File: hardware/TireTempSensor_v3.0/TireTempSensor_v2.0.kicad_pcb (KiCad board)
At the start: 4 copper layers, 27 x 54 mm, 57 parts, among them IC1 MAX15462AATA+, IC2 MLX90621ESF-BAB-000-SP, J1 SWD_01x06, J2 CAN_01x04, Q1 FQT3P20TF, SW1 RESET, U1 STM32L4P5RET6, U2 MIC5306-2.6YD5-TR, U3 SN65HVD232, Y1 16MGHz

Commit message: Piotruś prosił :3
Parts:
- removed F1: 200mA, Fuse:Fuse_1210_3225Metric
- removed FB4: 60R@100MHz, Inductor_SMD:L_0603_1608Metric
- removed the G*** at (102.5, 73.8)
- removed IC1: MAX15462AATA+, Package_DFN_QFN:TDFN-8-1EP_2x2mm_P0.5mm_EP0.8x1.2mm
- removed J1: SWD_01x06, Connector_PinHeader_2.54mm:PinHeader_1x06_P2.54mm_Vertical
- removed L1: 33μH, Inductor_SMD:L_Vishay_IFSC-1515AH_4x4x1.8mm
- removed R1: 100k, Resistor_SMD:R_0603_1608Metric
- added C26: 22u, Capacitor_SMD:C_0805_2012Metric_Pad1.18x1.45mm_HandSolder, F.Cu at (59.8, 179.4)
- added C27: 100n, Capacitor_SMD:C_0603_1608Metric_Pad1.08x0.95mm_HandSolder, F.Cu at (57.1, 178.9)
- added C28: 100n, Capacitor_SMD:C_0603_1608Metric_Pad1.08x0.95mm_HandSolder, F.Cu at (59.8, 181.2)
- added C29: 100n, Capacitor_SMD:C_0603_1608Metric_Pad1.08x0.95mm_HandSolder, F.Cu at (54.6, 176.0)
- added C32: 100n, Capacitor_SMD:C_0603_1608Metric_Pad1.08x0.95mm_HandSolder, F.Cu at (56.5, 124.8)
- added C33: 47u, Capacitor_SMD:C_0603_1608Metric_Pad1.08x0.95mm_HandSolder, F.Cu at (56.5, 127.3)
- added C34: 47u, Capacitor_SMD:C_0603_1608Metric_Pad1.08x0.95mm_HandSolder, F.Cu at (56.5, 129.8)
- added C35: 220n, Capacitor_SMD:C_0603_1608Metric_Pad1.08x0.95mm_HandSolder, F.Cu at (56.5, 132.3)
- added C36: 100n, Capacitor_SMD:C_0603_1608Metric_Pad1.08x0.95mm_HandSolder, F.Cu at (56.5, 134.8)
- added C37: 10n, Capacitor_SMD:C_0603_1608Metric_Pad1.08x0.95mm_HandSolder, F.Cu at (60.8, 124.8)
- added C38: 100n, Capacitor_SMD:C_0603_1608Metric_Pad1.08x0.95mm_HandSolder, F.Cu at (60.8, 127.3)
- added C39: 10n, Capacitor_SMD:C_0603_1608Metric_Pad1.08x0.95mm_HandSolder, F.Cu at (60.8, 129.8)
- added C40: 100n, Capacitor_SMD:C_0603_1608Metric_Pad1.08x0.95mm_HandSolder, F.Cu at (62.2, 184.5)
- added C41: 22u, Capacitor_SMD:C_0805_2012Metric_Pad1.18x1.45mm_HandSolder, F.Cu at (64.9, 183.8)
- added C42: 22u, Capacitor_SMD:C_0805_2012Metric_Pad1.18x1.45mm_HandSolder, F.Cu at (64.9, 185.8)
- added C43: 22u, Capacitor_SMD:C_0805_2012Metric_Pad1.18x1.45mm_HandSolder, F.Cu at (64.9, 187.8)
- added C44: 10u, Capacitor_SMD:C_0603_1608Metric_Pad1.08x0.95mm_HandSolder, F.Cu at (58.0, 176.1)
- added C45: 22u, Capacitor_SMD:C_0805_2012Metric_Pad1.18x1.45mm_HandSolder, F.Cu at (51.0, 175.8)
- added D10: D_TVS_Dual_AAC, Package_TO_SOT_SMD:SOT-23_Handsoldering, F.Cu at (72.1, 155.9)
- added D11: D_Zener, Diode_SMD:D_SOD-123, F.Cu at (82.3, 156.2)
- added D12: D_Zener, Diode_SMD:D_SOD-123, F.Cu at (82.3, 159.5)
- added D13: +3V3, LED_SMD:LED_0603_1608Metric_Pad1.05x0.95mm_HandSolder, F.Cu at (52.5, 184.8)
- added D7: D_TVS_Dual_AAC, Package_TO_SOT_SMD:SOT-23_Handsoldering, F.Cu at (72.1, 142.2)
- added D8: D_TVS_Dual_AAC, Package_TO_SOT_SMD:SOT-23_Handsoldering, F.Cu at (72.1, 146.8)
- added D9: D_TVS_Dual_AAC, Package_TO_SOT_SMD:SOT-23_Handsoldering, F.Cu at (72.1, 151.3)
- added F2: F0603G0R05FNTR, Fuse:Fuse_0603_1608Metric_Pad1.05x0.95mm_HandSolder, F.Cu at (56.0, 151.3)
- added F3: F0603G0R05FNTR, Fuse:Fuse_0603_1608Metric_Pad1.05x0.95mm_HandSolder, F.Cu at (48.3, 175.1)
- added F4: F0603G0R05FNTR, Fuse:Fuse_0603_1608Metric_Pad1.05x0.95mm_HandSolder, F.Cu at (54.6, 187.9)
- added F5: F0603G0R05FNTR, Fuse:Fuse_0603_1608Metric_Pad1.05x0.95mm_HandSolder, F.Cu at (59.7, 177.6)
- added FB5: 2K@100MHz, Inductor_SMD:L_0603_1608Metric_Pad1.05x0.95mm_HandSolder, F.Cu at (60.8, 132.3)
- added FB6: 2K@100MHz, Inductor_SMD:L_0603_1608Metric_Pad1.05x0.95mm_HandSolder, F.Cu at (60.8, 134.8)
- added FB7: 2K@100MHz, Inductor_SMD:L_0603_1608Metric_Pad1.05x0.95mm_HandSolder, F.Cu at (65.2, 124.8)
- added FB8: 2K@100MHz, Inductor_SMD:L_0603_1608Metric_Pad1.05x0.95mm_HandSolder, F.Cu at (65.2, 127.3)
- added IC4: TPS54202HDDCR, Package_TO_SOT_SMD:SOT-23-6_Handsoldering, F.Cu at (59.7, 184.3)
- added L4: 68u/1A4, Inductor_SMD:L_TDK_VLS6045EX_VLS6045AF, F.Cu at (65.0, 179.5)
- added R14: 1k, Resistor_SMD:R_0603_1608Metric_Pad0.98x0.95mm_HandSolder, F.Cu at (49.1, 184.8)
- added R15: 10k, Resistor_SMD:R_0603_1608Metric, F.Cu at (77.3, 141.2)
- added R16: 10k, Resistor_SMD:R_0603_1608Metric, F.Cu at (77.3, 143.7)
- added R17: 10k, Resistor_SMD:R_0603_1608Metric, F.Cu at (77.3, 146.2)
- added R18: 1k, Resistor_SMD:R_0603_1608Metric, F.Cu at (77.3, 148.8)
- added R19: 1k, Resistor_SMD:R_0603_1608Metric, F.Cu at (77.3, 151.3)
- added R20: 1k, Resistor_SMD:R_0603_1608Metric, F.Cu at (77.3, 153.8)
- added R21: 100K, Resistor_SMD:R_0603_1608Metric_Pad0.98x0.95mm_HandSolder, F.Cu at (65.2, 129.8)
- added R22: 510k, Resistor_SMD:R_0603_1608Metric_Pad0.98x0.95mm_HandSolder, F.Cu at (57.1, 184.5)
- added R23: 13.2k, Resistor_SMD:R_0603_1608Metric_Pad0.98x0.95mm_HandSolder, F.Cu at (58.0, 187.5)
- added R24: 100k, Resistor_SMD:R_0603_1608Metric_Pad0.98x0.95mm_HandSolder, F.Cu at (61.3, 187.5)
- added SW2: 3 pos dip switch, footprint:DS04254103BKSMT, F.Cu at (85.6, 146.9)
- added T10: TP_+5V, TestPoint:TestPoint_Pad_1.0x1.0mm, B.Cu at (59.6, 177.8)
- added T12: TP_+5V, TestPoint:TestPoint_Pad_1.0x1.0mm, B.Cu at (63.9, 187.8)
- added T13: TP_+5V, TestPoint:TestPoint_Pad_1.0x1.0mm, F.Cu at (58.4, 154.1)
- added T14: TP_+3.3V, TestPoint:TestPoint_Pad_1.0x1.0mm, B.Cu at (50.0, 173.9)
- added T15: TP_+2.6V, TestPoint:TestPoint_Pad_1.0x1.0mm, B.Cu at (55.5, 189.6)
- added U7: ADM3057ExRW, Package_SO:SOIC-20W_7.5x12.8mm_P1.27mm, F.Cu at (30.9, 139.7)
- C12, C13: value 1u -> 100n
- C16: value 10u -> 100n; footprint Capacitor_SMD:C_1206_3216Metric -> Capacitor_SMD:C_0603_1608Metric
- D1: value PESD2CAN,215 -> 30V; footprint Package_TO_SOT_SMD:SOT-23 -> Diode_SMD:D_SOD-123
- IC2: moved to F.Cu
- U1: value STM32L4P5RET6 -> STM32G0C1KCTxN; footprint Package_QFP:LQFP-64_10x10mm_P0.5mm -> Package_QFP:LQFP-32_7x7mm_P0.8mm
- U3: value SN65HVD232 -> LM1117-3.3; footprint Package_SO:SOIC-8_3.9x4.9mm_P1.27mm -> Package_TO_SOT_SMD:SOT-223-3_TabPin2
- moved C14 136.4 mm to (48.9, 189.5), turned to 0 degrees
- moved U2 132.7 mm to (50.8, 187.3), turned to 0 degrees
- moved FB2 132.0 mm to (48.0, 187.3), turned to -90 degrees
- moved C15 128.3 mm to (54.4, 186.4), turned to 0 degrees
- moved U3 95.0 mm to (51.9, 180.4), turned to 180 degrees
- moved U1 80.1 mm to (40.8, 118.0), turned to -135 degrees
- moved C16 55.5 mm to (80.3, 69.8), turned to 0 degrees
- moved J2 53.9 mm to (72.1, 85.4), turned to 0 degrees
- moved H1 49.4 mm to (96.1, 71.5)
- moved C13 49.3 mm to (76.3, 82.3)
- moved C4 48.5 mm to (72.3, 77.3), turned to 0 degrees
- moved IC2 48.3 mm to (79.0, 101.4), turned to 0 degrees
- moved R6 47.4 mm to (84.7, 104.0), turned to 0 degrees
- moved C11 47.4 mm to (76.3, 77.3), turned to 0 degrees
- moved C12 47.3 mm to (76.3, 79.8)
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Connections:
- C12 pad 1: /Power Supply 3.3v 2.6v/+24V safe -> /Switch1
- C13 pad 1: Net-(C13-Pad1) -> /Switch2
- C15 pad 1: +2V6 -> Net-(U2-VOUT)
- C16 pad 1: +3V3 -> /Switch3
- D1 pad 1: /CAN - -> +24V
- D1 pad 2: /CAN + -> GND
- JP1 pad 1: Net-(F1-Pad2) -> Net-(JP1-A)
- U1 pad 1: /+3V3_uC -> unconnected-(U1-PB9-Pad1)
- U1 pad 12: GND -> /LED OK
- U1 pad 13: /+3V3_uC -> /LED ERR
- U1 pad 14: unconnected-(U1-Pad14) -> /LED WAR1
- U1 pad 16: /LED WAR2 -> unconnected-(U1-PB1-Pad16)
- U1 pad 18: GND -> /LED WAR2
- U1 pad 19: /+3V3_uC -> /Switch1
- U1 pad 2: unconnected-(U1-Pad2) -> /OSC IN
- U1 pad 20: unconnected-(U1-Pad20) -> /+3V3_uC
- U1 pad 21: unconnected-(U1-Pad21) -> /Switch2
- U1 pad 22: /LED ERR -> /Switch3
- U1 pad 24: /LED WAR1 -> /SWDIO
- U1 pad 25: unconnected-(U1-Pad25) -> /SWCLK
- U1 pad 26: /LED OK -> /STBY_CAN
- U1 pad 29: /SCL -> unconnected-(U1-PD3-Pad29)
- U1 pad 3: unconnected-(U1-Pad3) -> /OSC OUT
- U1 pad 30: /SDA -> unconnected-(U1-PB6-Pad30)
- U1 pad 31: GND -> unconnected-(U1-PB7-Pad31)
- U1 pad 32: /+3V3_uC -> unconnected-(U1-PB8-Pad32)
- U1 pad 4: unconnected-(U1-Pad4) -> /+3V3_uC
- U1 pad 5: /OSC IN -> GND
- U1 pad 6: /OSC OUT -> /NRST
- U1 pad 7: /NRST -> unconnected-(U1-PA0-Pad7)
- U1 pad 8: unconnected-(U1-Pad8) -> /SCL
- U1 pad 9: unconnected-(U1-Pad9) -> /SDA
- U2 pad 5: +2V6 -> Net-(U2-VOUT)
- U3 pad 1: /CAN TX -> GND
- U3 pad 2: GND -> /Power Supply 3.3v 2.6v/VO_+3.3V
- U3 pad 3: Net-(FB4-Pad2) -> +5V
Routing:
- net GND: track 54.2 -> 0.00 mm, vias 42 -> 0
- net /SWO: track 30.5 -> 0.00 mm
- net /CAN RX: track 30.5 -> 0.00 mm, vias 2 -> 0
- net /NRST: track 29.3 -> 0.00 mm
- net /CAN TX: track 27.7 -> 0.00 mm, vias 2 -> 0
- net /SCL: track 25.8 -> 0.00 mm, vias 2 -> 0
- net /SDA: track 24.7 -> 0.00 mm, vias 2 -> 0
- net /+3V3_uC: track 20.4 -> 0.00 mm, vias 8 -> 0
- net /CAN +: track 16.7 -> 0.00 mm
- net /CAN -: track 15.4 -> 0.00 mm
- net +2V6: track 12.9 -> 0.00 mm
- net /SWDIO: track 12.4 -> 0.00 mm
- net /SWCLK: track 12.0 -> 0.00 mm, vias 2 -> 0
- net /OSC IN: track 10.5 -> 0.00 mm
- net /LED OK: track 10.3 -> 0.00 mm
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- removed copper zone on F.Cu, net +3V3
- removed copper zone on In2.Cu, net +3V3
- removed copper zone on In2.Cu, net /+3V3_uC
- removed copper zone on F.Cu, net /Power Supply 3.3v 2.6v/+24V safe
- removed copper zone on B.Cu, net GND
- removed copper zone on F.Cu, net GND
- removed copper zone on In1.Cu, net GND
- removed copper zone on F.Cu, net Net-(C13-Pad1)
- removed copper zone on F.Cu, net Net-(F1-Pad2)
- removed copper zone on F.Cu, net Net-(IC1-Pad8)
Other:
- board size 27 x 54 mm -> 25.8 x 20.6 mm

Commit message: Poprawki, kontynuacja layoutu
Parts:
- removed C16: 100n, Capacitor_SMD:C_0603_1608Metric
- removed R17: 10k, Resistor_SMD:R_0603_1608Metric
- removed R20: 1k, Resistor_SMD:R_0603_1608Metric
- removed SW2: 3 pos dip switch, footprint:DS04254103BKSMT
- added D14: D_TVS_Dual_AAC, Package_TO_SOT_SMD:SOT-23_Handsoldering, F.Cu at (128.3, 100.1)
- added D15: D_TVS_Dual_AAC, Package_TO_SOT_SMD:SOT-23_Handsoldering, F.Cu at (132.9, 101.0)
- added J3: FTSH-107-01-L-D-K, footprint:FTSH-107-XX-YYY-DV-K, F.Cu at (131.2, 93.8)
- added SW3: SW_DIP_x02, footprint:2192LPST, B.Cu at (155.3, 99.6)
- C32, C38: value 100n -> 47u
- C35: value 220n -> 47u
- IC2, R15, R16, R18, R19: moved to B.Cu
- J2: value CAN_01x04 -> Main connector; footprint Connector_Wire:SolderWire-0.1sqmm_1x04_P3.6mm_D0.4mm_OD1mm_Relief -> footprint:M80-51004YY
- Q1: footprint Mosfet:SOT-223-4-NFET -> Package_TO_SOT_SMD:SOT-223-3_TabPin2
- moved F3 140.4 mm to (161.7, 92.3), turned to 180 degrees
- moved T10 139.3 mm to (172.3, 96.0)
- moved T12 139.3 mm to (176.7, 106.0)
- moved T15 139.3 mm to (168.2, 107.8)
- moved C26 139.3 mm to (172.5, 97.7)
- moved C27 139.3 mm to (169.8, 97.1)
- moved C45 139.3 mm to (163.7, 94.0)
- moved D13 139.3 mm to (165.2, 103.0)
- moved F5 139.3 mm to (172.4, 95.8)
- moved FB2 139.3 mm to (160.7, 105.5)
- moved IC4 139.3 mm to (172.4, 102.6)
- moved R14 139.3 mm to (161.8, 103.0)
- moved U2 139.3 mm to (163.5, 105.5)
- moved C14 139.3 mm to (161.6, 107.8)
- moved C15 139.3 mm to (167.2, 104.7)
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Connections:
- D10 pad 1: /OSC IN -> /OSC OUT
- D10 pad 2: /OSC OUT -> /OSC IN
- D7 pad 1: /SCL -> /SDA
- D7 pad 2: /SDA -> /SCL
- D8 pad 1: /SWDIO -> /SWCLK
- D8 pad 2: /SWCLK -> /SWDIO
- J2 pad 3: /CAN + -> /CAN -
- J2 pad 4: /CAN - -> /CAN +
- U1 pad 1: unconnected-(U1-PB9-Pad1) -> /CAN TX
- U1 pad 10: unconnected-(U1-PA3-Pad10) -> /LED OK
- U1 pad 11: unconnected-(U1-PA4-Pad11) -> /LED ERR
- U1 pad 12: /LED OK -> /LED WAR1
- U1 pad 13: /LED ERR -> /LED WAR2
- U1 pad 14: /LED WAR1 -> unconnected-(U1-PA7-Pad14)
- U1 pad 18: /LED WAR2 -> unconnected-(U1-PA8-Pad18)
- U1 pad 22: /Switch3 -> /CAN RX
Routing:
- net /Power Supply 3.3v 2.6v/+24V safe: track 0.00 -> 35.7 mm, vias 0 -> 2
- net /+3V3_uC: track 0.00 -> 21.0 mm
- net /SDA: track 0.00 -> 16.8 mm
- net /SCL: track 0.00 -> 16.0 mm
- net /NRST: track 0.00 -> 15.6 mm
- net /OSC OUT: track 0.00 -> 13.2 mm
- net /Power Supply 3.3v 2.6v/VO_+3.3V: track 0.00 -> 13.0 mm
- net /Power Supply 3.3v 2.6v/+5V_OUT: track 0.00 -> 12.6 mm, vias 0 -> 1
- net /OSC IN: track 0.00 -> 12.1 mm
- net +3V3: track 0.00 -> 9.59 mm
- net /Power Supply 3.3v 2.6v/SW_+5V: track 0.00 -> 8.44 mm
- net Net-(R3-Pad1): track 0.00 -> 7.31 mm
- net Net-(U2-EN): track 0.00 -> 6.91 mm
- net /SWDIO: track 0.00 -> 6.23 mm
- net /Switch2: track 0.00 -> 6.05 mm
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- added copper zone on F.Cu, net /Power Supply 3.3v 2.6v/+5V_OUT
- added copper zone on F.Cu, net /Power Supply 3.3v 2.6v/VO_+3.3V
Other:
- board outline removed

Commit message: Propozycja layoutu na spotkanie
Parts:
- removed D3, D4: YELLOW, Diode_SMD:D_0603_1608Metric
- removed D6: RED, Diode_SMD:D_0603_1608Metric
- removed JP1: SolderJumper_2_Open, Jumper:SolderJumper-2_P1.3mm_Open_TrianglePad1.0x1.5mm
- removed Q1: FQT3P20TF, Package_TO_SOT_SMD:SOT-223-3_TabPin2
- removed R10, R7, R8: 1k5, Resistor_SMD:R_0603_1608Metric
- added D16: D_Schottky, Diode_SMD:D_SOD-882D, F.Cu at (177.2, 108.2)
- T13: moved to B.Cu
- moved C33 76.9 mm to (129.7, 103.8), turned to 90 degrees
- moved C32 73.8 mm to (127.3, 104.2)
- moved C38 70.0 mm to (127.7, 106.6)
- moved T13 68.3 mm to (127.7, 106.6)
- moved FB7 65.9 mm to (127.3, 102.7)
- moved C36 64.7 mm to (111.3, 100.6)
- moved C39 64.5 mm to (121.0, 106.6), turned to 180 degrees
- moved C34 62.9 mm to (111.3, 99.1), turned to 180 degrees
- moved FB8 62.7 mm to (124.4, 106.6)
- moved C35 61.9 mm to (111.3, 103.6)
- moved C37 60.0 mm to (111.4, 92.5)
- moved FB5 58.9 mm to (111.3, 102.1), turned to 180 degrees
- moved FB6 58.6 mm to (111.4, 105.1)
- moved R21 58.5 mm to (111.4, 94.0)
- moved R6 54.6 mm to (139.2, 100.7)
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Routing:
- net /Power Supply 3.3v 2.6v/+24V safe: track 35.7 -> 19.2 mm
- net Net-(D16-A): track 4.63 -> 1.87 mm
- net /NRST: track 15.6 -> 17.0 mm
- net /SDA: track 16.8 -> 16.2 mm
- added copper zone on B.Cu, net GND
- added copper zone on F.Cu, net GND
- added copper zone on In1.Cu, net GND
- added copper zone on In2.Cu, net GND
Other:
- board outline added: 82.5 x 20.6 mm

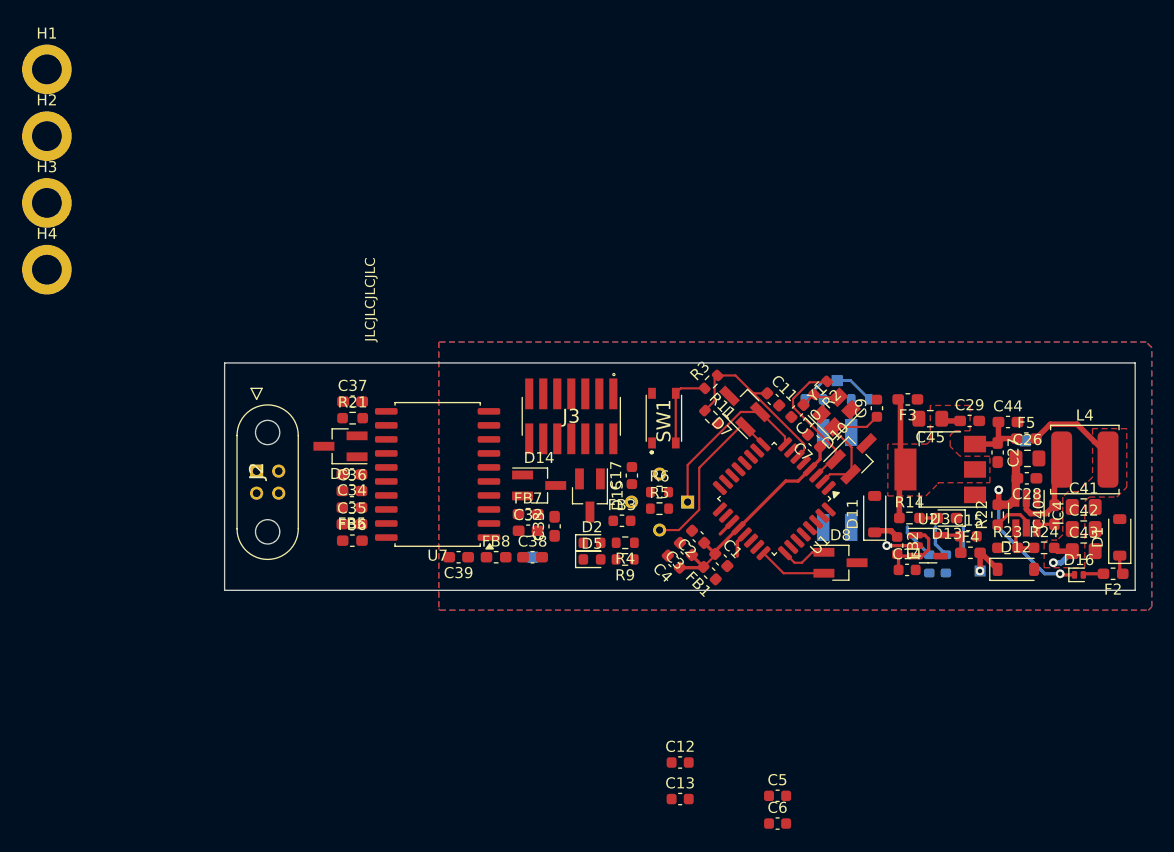
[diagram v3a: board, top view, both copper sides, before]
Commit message: Nowy layout, nowe tvsy
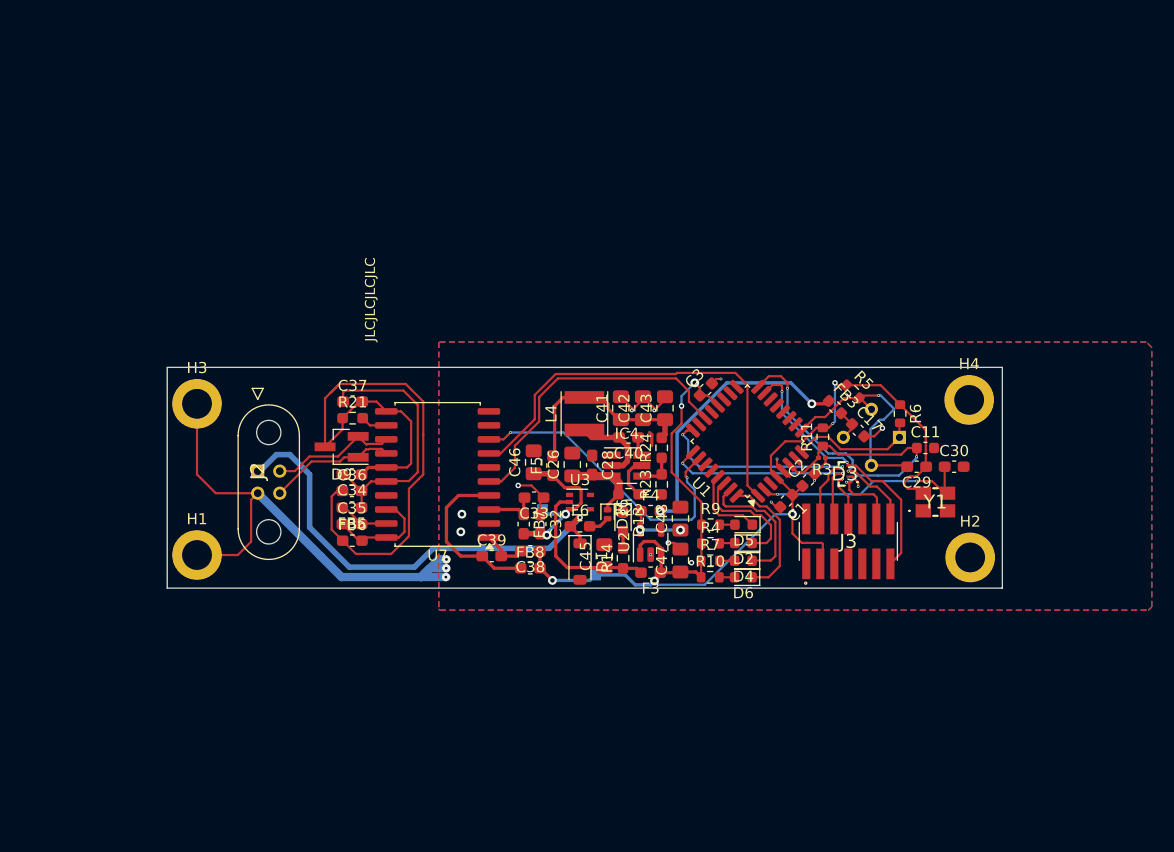
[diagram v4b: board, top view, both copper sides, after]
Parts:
- removed C10, C9: 8p, Capacitor_SMD:C_0603_1608Metric
- removed C12, C13, C14, C15, C4, C5, C6, C7: 100n, Capacitor_SMD:C_0603_1608Metric
- removed C27: 100n, Capacitor_SMD:C_0603_1608Metric_Pad1.08x0.95mm_HandSolder
- removed C44: 10u, Capacitor_SMD:C_0603_1608Metric_Pad1.08x0.95mm_HandSolder
- removed D10, D14, D15, D7, D8: D_TVS_Dual_AAC, Package_TO_SOT_SMD:SOT-23_Handsoldering
- removed D11, D12: D_Zener, Diode_SMD:D_SOD-123
- removed F2: F0603G0R05FNTR, Fuse:Fuse_0603_1608Metric_Pad1.05x0.95mm_HandSolder
- removed FB1, FB2: 60R@100MHz, Inductor_SMD:L_0603_1608Metric
- removed R15, R16: 10k, Resistor_SMD:R_0603_1608Metric
- removed R18, R19: 1k, Resistor_SMD:R_0603_1608Metric
- removed R2: 47, Resistor_SMD:R_0603_1608Metric
- removed SW1: RESET, Button:PTS815SJK250SMTRLFS
- removed SW3: SW_DIP_x02, footprint:2192LPST
- removed T12, T13: TP_+5V, TestPoint:TestPoint_Pad_1.0x1.0mm
- added C30: 6p, Capacitor_SMD:C_0603_1608Metric_Pad1.08x0.95mm_HandSolder, F.Cu at (165.9, 98.4)
- added C46: 22u, Capacitor_SMD:C_0805_2012Metric_Pad1.18x1.45mm_HandSolder, F.Cu at (127.8, 98.0)
- added C47: 22u, Capacitor_SMD:C_0805_2012Metric_Pad1.18x1.45mm_HandSolder, F.Cu at (141.1, 106.9)
- added C48: 22u, Capacitor_SMD:C_0805_2012Metric_Pad1.18x1.45mm_HandSolder, F.Cu at (141.1, 103.1)
- added D3: PUSB3AB6Z, footprint:PUSB3AB6Z, F.Cu at (156.0, 99.0)
- added D4: RED, Diode_SMD:D_0603_1608Metric, F.Cu at (146.8, 106.9)
- added D6: GREEN, Diode_SMD:D_0603_1608Metric, F.Cu at (146.8, 108.4)
- added F6: SF-0603FP050M-2, Fuse:Fuse_0603_1608Metric_Pad1.05x0.95mm_HandSolder, F.Cu at (132.0, 103.8)
- added R10: 1k5, Resistor_SMD:R_0603_1608Metric, F.Cu at (143.8, 108.4)
- added R7: 1k5, Resistor_SMD:R_0603_1608Metric, F.Cu at (143.8, 106.9)
- C29: value 100n -> 100nF
- F5: value F0603G0R05FNTR -> SF-0603FP050M-2
- L4: footprint Inductor_SMD:L_TDK_VLS6045EX_VLS6045AF -> Inductor_SMD:L_Vishay_IFSC-1515AH_4x4x1.8mm
- R3: value 1k -> NC; footprint Resistor_SMD:R_0603_1608Metric -> Resistor_SMD:R_0201_0603Metric
- U3: value LM1117-3.3 -> NCP715SQ33T2G; footprint Package_TO_SOT_SMD:SOT-223-3_TabPin2 -> Package_TO_SOT_SMD:SOT-353_SC-70-5
- Y1: value 16MGHz -> ATX-11-F-32.000MHZ-F05-T; footprint Crystal:Crystal_SMD_SeikoEpson_TSX3225-4Pin_3.2x2.5mm -> footprint:ATX11F32000MHZF05T
- moved H2 91.9 mm to (167.3, 106.6)
- moved H4 84.4 mm to (167.3, 92.3)
- moved D1 48.9 mm to (132.0, 107.0), turned to -90 degrees
- moved H1 46.1 mm to (97.3, 106.4)
- moved L4 45.5 mm to (132.4, 93.6), turned to 90 degrees
- moved T10 44.2 mm to (128.6, 102.3)
- moved D16 43.1 mm to (134.5, 102.7), turned to -90 degrees
- moved F5 43.0 mm to (129.5, 98.3), turned to 90 degrees
- moved C41 42.9 mm to (135.7, 93.1), turned to 90 degrees
- moved C42 41.4 mm to (137.7, 93.1), turned to 90 degrees
- moved C26 41.2 mm to (131.3, 98.2), turned to 90 degrees
- moved C43 40.1 mm to (139.7, 93.1), turned to 90 degrees
- moved C28 39.4 mm to (133.1, 98.2), turned to -90 degrees
- moved C40 39.2 mm to (136.4, 95.8), turned to 180 degrees
- moved IC4 36.4 mm to (136.2, 98.3), turned to 0 degrees
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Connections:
- C1 pad 1: /+3V3_uC -> +3V3
- C2 pad 1: /+3V3_uC -> +3V3
- C29 pad 1: /Power Supply 3.3v 2.6v/VO_+3.3V -> +3V3
- C3 pad 1: /+3V3_uC -> +3V3
- C38 pad 1: +3.3V -> +3V3
- D2 pad 1: GND -> /LED ERR
- D5 pad 1: GND -> /LED OK
- FB8 pad 2: +3.3V -> +3V3
- J3 pad 13: unconnected-(J3-Pin_13-Pad13) -> /URAT_RX
- J3 pad 14: unconnected-(J3-Pin_14-Pad14) -> /URAT_TX
- J3 pad 3: +3.3V -> +3V3
- R3 pad 1: Net-(R3-Pad1) -> GND
- R4 pad 1: /LED ERR -> +3V3
- R9 pad 1: /LED OK -> +3V3
- U1 pad 10: /LED OK -> unconnected-(U1-PA3-Pad10)
- U1 pad 11: /LED ERR -> unconnected-(U1-PA4-Pad11)
- U1 pad 15: unconnected-(U1-PB0-Pad15) -> /URAT_RX
- U1 pad 16: unconnected-(U1-PB1-Pad16) -> /URAT_TX
- U1 pad 20: /+3V3_uC -> +3V3
- U1 pad 29: unconnected-(U1-PD3-Pad29) -> /LED OK
- U1 pad 30: unconnected-(U1-PB6-Pad30) -> /LED ERR
- U1 pad 31: unconnected-(U1-PB7-Pad31) -> /LED_ADRESS_INDICATOR_1
- U1 pad 32: unconnected-(U1-PB8-Pad32) -> /LED_ADRESS_INDICATOR_2
- U1 pad 4: /+3V3_uC -> +3V3
- U2 pad 1: Net-(U2-EN) -> +3V3
- U2 pad 3: Net-(U2-EN) -> +3V3
- Y1 pad 1: /OSC IN -> GND
- Y1 pad 3: Net-(C10-Pad1) -> /OSC IN
- Y1 pad 4: GND -> +3V3
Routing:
- net +3V3: track 9.59 -> 105.3 mm, vias 0 -> 7
- net GND: track 2.61 -> 79.4 mm, vias 1 -> 18
- net /GND_ISO: track 0.00 -> 60.5 mm
- net +24V: track 1.76 -> 41.8 mm, vias 0 -> 1
- net /CAN TX: track 0.00 -> 38.6 mm
- net /STBY_CAN: track 0.00 -> 28.4 mm, vias 0 -> 2
- net /CAN RX: track 0.00 -> 28.0 mm
- net /URAT_RX: track 0.00 -> 24.7 mm, vias 0 -> 2
- net Net-(U7-VISOIN): track 0.00 -> 24.0 mm
- net +2V6: track 3.86 -> 25.5 mm, vias 1 -> 2
- net /URAT_TX: track 0.00 -> 21.5 mm, vias 0 -> 2
- net /+3V3_uC: track 21.0 -> 0.00 mm
- net /SWDIO: track 6.23 -> 23.5 mm, vias 0 -> 2
- net /SWCLK: track 4.28 -> 21.1 mm, vias 0 -> 2
- net Net-(U7-VIO): track 0.00 -> 15.1 mm
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- removed copper zone on F.Cu, net /Power Supply 3.3v 2.6v/+5V_OUT
- removed copper zone on F.Cu, net /Power Supply 3.3v 2.6v/VO_+3.3V
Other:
- board size 82.5 x 20.6 mm -> 75.7 x 20 mm
- board text added: "Wiktor Krakowski :3"

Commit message: Gotowe do sprawdzenia
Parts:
- R3: footprint Resistor_SMD:R_0201_0603Metric -> Resistor_SMD:R_0402_1005Metric
- moved C1 1.33 mm to (150.9, 102.8), turned to -90 degrees
- moved R3 1.27 mm to (153.3, 98.7), turned to 135 degrees
- moved H1 1.26 mm to (98.5, 106.0)
- moved H3 1.20 mm to (98.5, 92.7)
- moved C2 1.05 mm to (152.3, 100.6), turned to 0 degrees
- moved Y1 0.55 mm to (164.8, 101.6)
- moved C48 0.14 mm to (141.2, 103.1)
- moved F5 0.06 mm to (129.6, 98.3)
- moved D13 0.06 mm to (136.0, 103.4)
- moved R14 0.05 mm to (135.9, 106.8)
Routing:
- net GND: track 79.4 -> 82.8 mm, vias 18 -> 25
- net /SDA: track 18.0 -> 16.5 mm
- net +24V: track 41.8 -> 40.7 mm
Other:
- board size 75.7 x 20 mm -> 75 x 20.5 mm
- board text added: "bridge to rst"

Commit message: Do sprawdzenia :3
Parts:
- moved G*** 4.97 mm to (118.5, 95.5)
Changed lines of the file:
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@@
 		(tags "SOT-23")
 		(property "Reference" "D9"
-			(at 2.25 -0.11 180)
+			(at 2.4 1.1 180)
 			(layer "F.SilkS")
 			(effects
@@
 		(tags "test point SMD pad rectangle square")
 		(property "Reference" "T10"
-			(at 2.4 0.7 180)
+			(at 2.4 0.2 180)
 			(layer "B.SilkS")
 			(effects
@@
 		(tags "test point SMD pad rectangle square")
 		(property "Reference" "T14"
-			(at 0 1.448 180)
+			(at -2.4 -0.2 180)
 			(layer "B.SilkS")
 			(effects
@@
 	(footprint "mylogo:logo"
 		(layer "B.Cu")
-		(at 120.6 100 180)
+		(at 118.5 95.5 180)
 		(property "Reference" "G***"
 			(at -0.5 4.75 0)
@@
 		(tags "test point SMD pad rectangle square")
 		(property "Reference" "T15"
-			(at 0 1.448 180)
+			(at -2.2 -0.1 180)
 			(layer "B.SilkS")
 			(effects
@@
 	)
 	(gr_line
-		(start 120.5 104.5)
-		(end 121.5 105.5)
+		(start 117.5 100)
+		(end 118.5 101)
 		(stroke
 			(width 0.15)
@@
 	)
 	(gr_line
-		(start 120.5 105.5)
-		(end 121.5 104.5)
+		(start 117.5 101)
+		(end 118.5 100)
 		(stroke
 			(width 0.15)
@@
 	)
 	(gr_text "Wiktor Krakowski :3"
-		(at 127.5 107 0)
+		(at 125.5 102.5 0)
 		(layer "B.SilkS")
 		(effects
